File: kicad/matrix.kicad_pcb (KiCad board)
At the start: 2 copper layers, 7 parts, among them U1 TLC59025, U2 74HC595, U3 74HC595

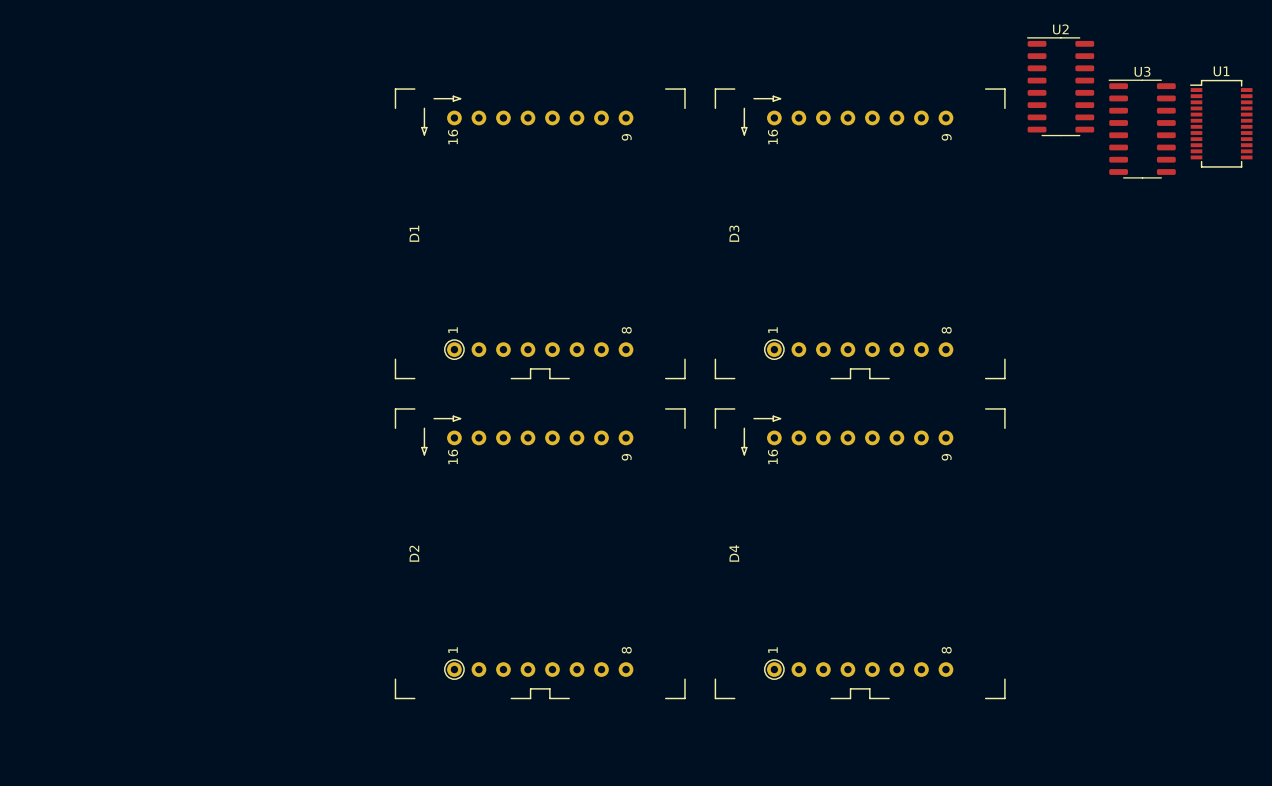
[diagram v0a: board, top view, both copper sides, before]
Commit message: Add footprints and initial layout
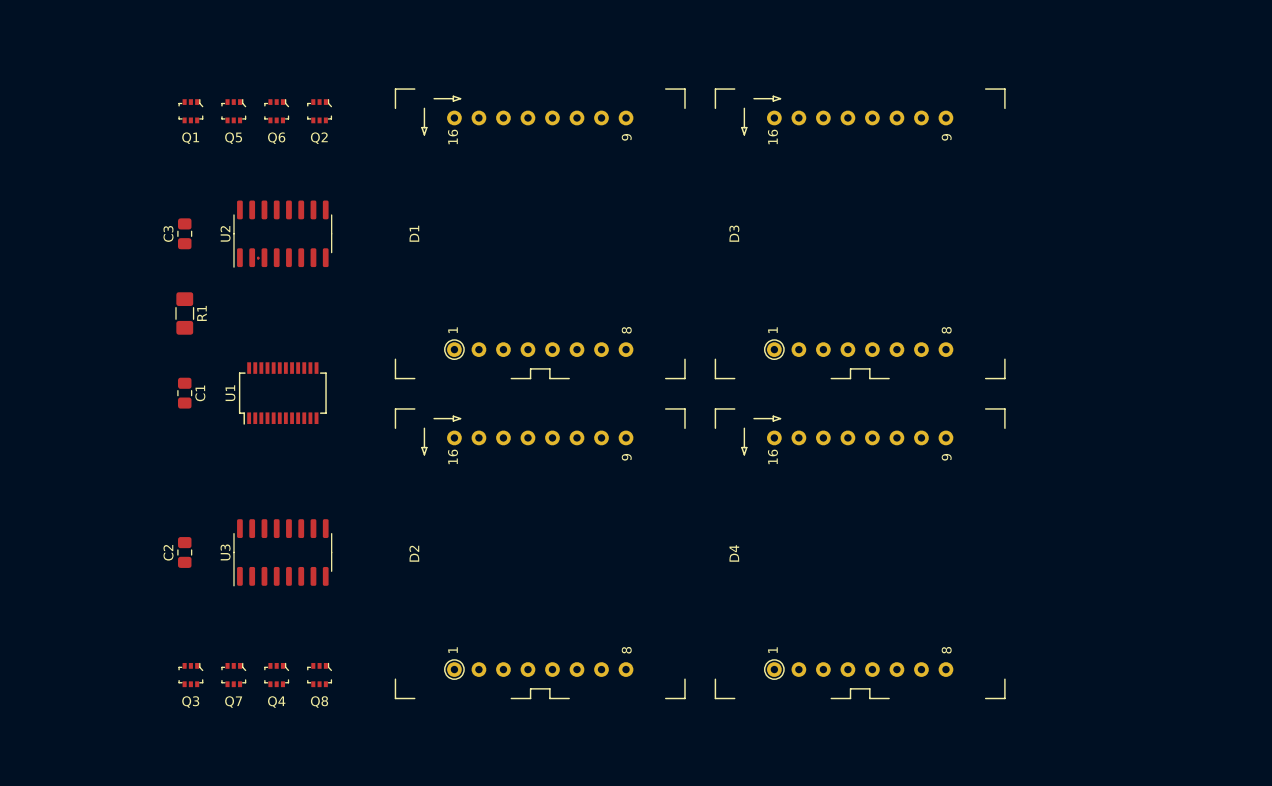
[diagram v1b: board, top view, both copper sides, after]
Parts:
- added C1: 100nF, Capacitor_SMD:C_0805_2012Metric_Pad1.15x1.40mm_HandSolder, F.Cu at (131.4, 75.6)
- added C2: 100nF, Capacitor_SMD:C_0805_2012Metric_Pad1.15x1.40mm_HandSolder, F.Cu at (131.4, 92.1)
- added C3: 100nF, Capacitor_SMD:C_0805_2012Metric_Pad1.15x1.40mm_HandSolder, F.Cu at (131.4, 59.1)
- added Q1: 2N7002DW-7-F, digikey-footprints:SOT-363, F.Cu at (132.1, 46.4)
- added Q2: 2N7002DW-7-F, digikey-footprints:SOT-363, F.Cu at (145.4, 46.4)
- added Q3: 2N7002DW-7-F, digikey-footprints:SOT-363, F.Cu at (132.1, 104.8)
- added Q4: 2N7002DW-7-F, digikey-footprints:SOT-363, F.Cu at (141.0, 104.8)
- added Q5: 2N7002DW-7-F, digikey-footprints:SOT-363, F.Cu at (136.5, 46.4)
- added Q6: 2N7002DW-7-F, digikey-footprints:SOT-363, F.Cu at (141.0, 46.4)
- added Q7: 2N7002DW-7-F, digikey-footprints:SOT-363, F.Cu at (136.5, 104.8)
- added Q8: 2N7002DW-7-F, digikey-footprints:SOT-363, F.Cu at (145.4, 104.8)
- added R1: 2.2K, Resistor_SMD:R_1206_3216Metric_Pad1.42x1.75mm_HandSolder, F.Cu at (131.4, 67.3)
- moved U1 101.2 mm to (141.6, 75.6), turned to 90 degrees
- moved U3 99.3 mm to (141.6, 92.1), turned to 90 degrees
- moved U2 82.0 mm to (141.6, 59.1), turned to 90 degrees
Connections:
- U2 pad 1: /ROW2 -> Net-(Q5-Pad2)
- U2 pad 15: /ROW1 -> Net-(Q1-Pad2)
- U2 pad 2: /ROW3 -> Net-(Q1-Pad5)
- U2 pad 3: /ROW4 -> Net-(Q5-Pad5)
- U2 pad 4: /ROW5 -> Net-(Q6-Pad2)
- U2 pad 5: /ROW6 -> Net-(Q2-Pad2)
- U2 pad 6: /ROW7 -> Net-(Q2-Pad5)
- U2 pad 7: /ROW8 -> Net-(Q6-Pad5)
- U3 pad 1: /ROW10 -> Net-(Q7-Pad2)
- U3 pad 15: /ROW9 -> Net-(Q3-Pad2)
- U3 pad 2: /ROW11 -> Net-(Q3-Pad5)
- U3 pad 3: /ROW12 -> Net-(Q7-Pad5)
- U3 pad 4: /ROW13 -> Net-(Q8-Pad2)
- U3 pad 5: /ROW14 -> Net-(Q4-Pad2)
- U3 pad 6: /ROW15 -> Net-(Q4-Pad5)
- U3 pad 7: /ROW16 -> Net-(Q8-Pad5)

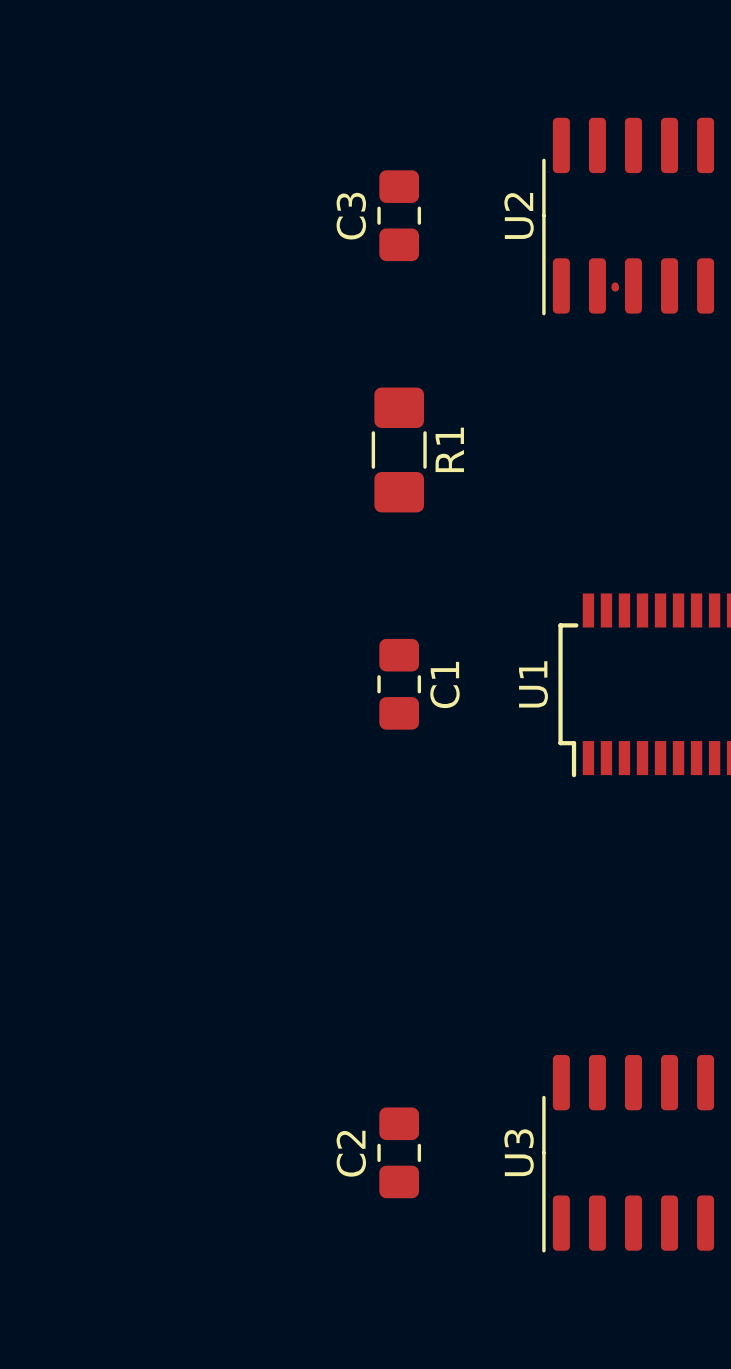
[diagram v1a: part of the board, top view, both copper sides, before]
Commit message: Add headers to PCB layout
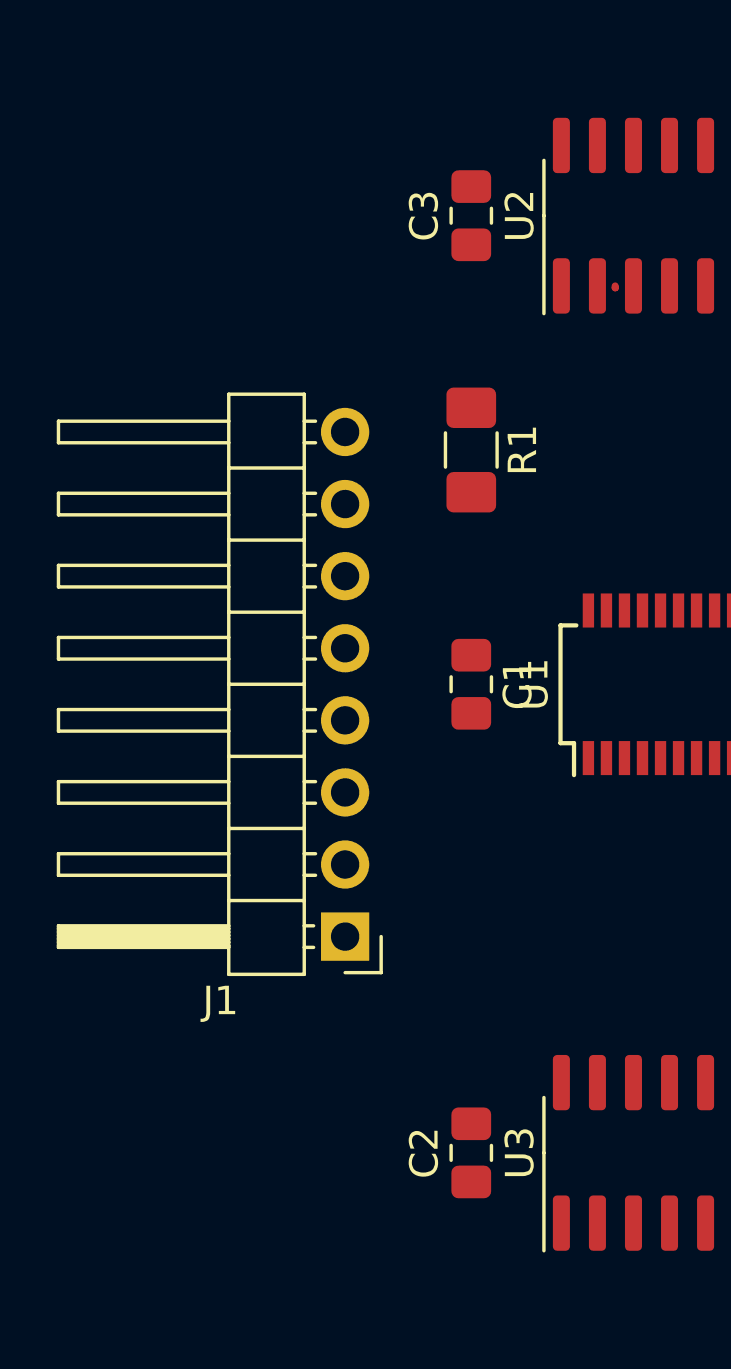
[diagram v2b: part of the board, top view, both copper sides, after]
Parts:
- added J1: Conn_01x08, Connector_PinHeader_2.54mm:PinHeader_1x08_P2.54mm_Horizontal, F.Cu at (129.5, 84.5)
- moved C1 2.54 mm to (134.0, 75.6)
- moved C2 2.54 mm to (134.0, 92.1)
- moved C3 2.54 mm to (134.0, 59.1)
- moved R1 2.54 mm to (134.0, 67.3)
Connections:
- net Net-(U2-Pad11) renamed /ROWCLK
- U1 pad 2: Net-(U1-Pad2) -> /COLSDI
- U1 pad 3: Net-(U1-Pad3) -> /COLCLK
- U1 pad 4: Net-(U1-Pad4) -> /LE
- U2 pad 10: Net-(U2-Pad10) -> VDD
- U2 pad 12: Net-(U2-Pad12) -> /LE
- U2 pad 14: Net-(U2-Pad14) -> /ROWSDI
- U3 pad 10: Net-(U2-Pad10) -> VDD
- U3 pad 12: Net-(U3-Pad12) -> /LE

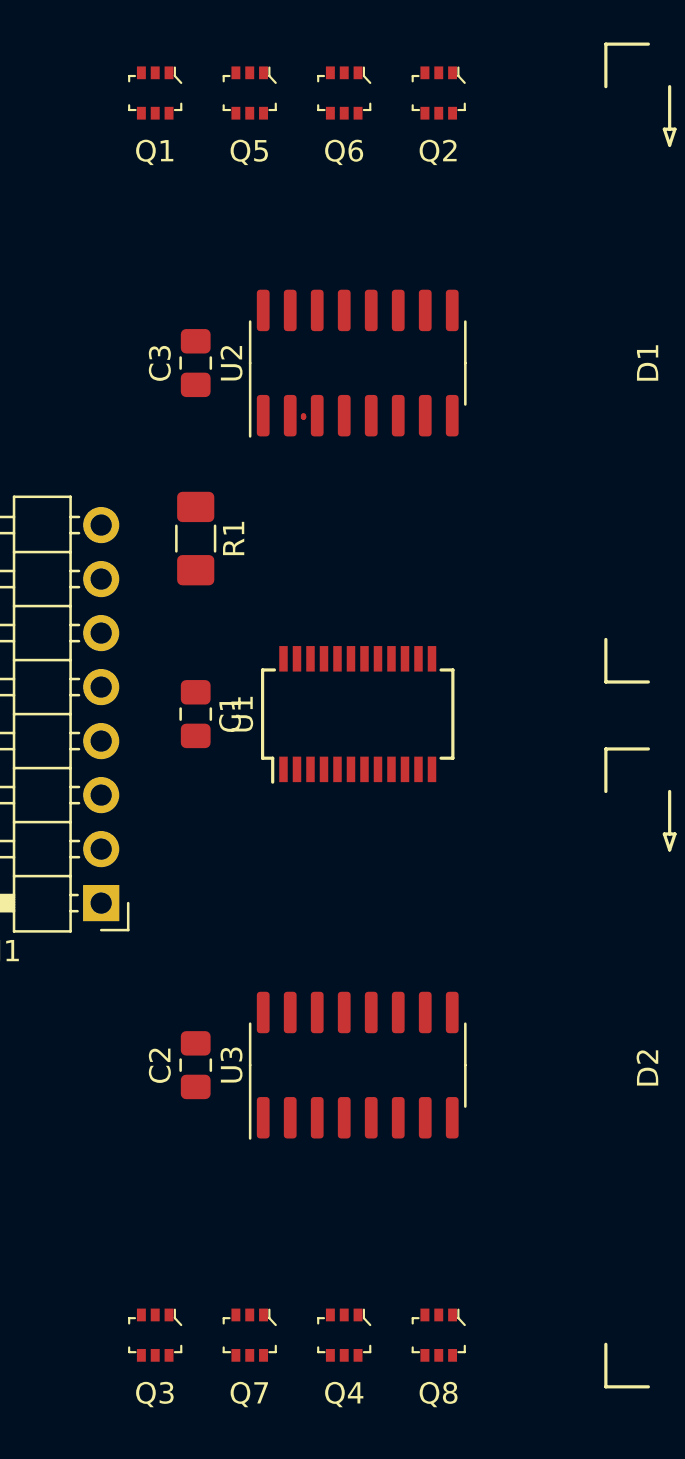
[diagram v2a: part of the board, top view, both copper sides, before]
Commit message: Add datasheets and long pad footprints
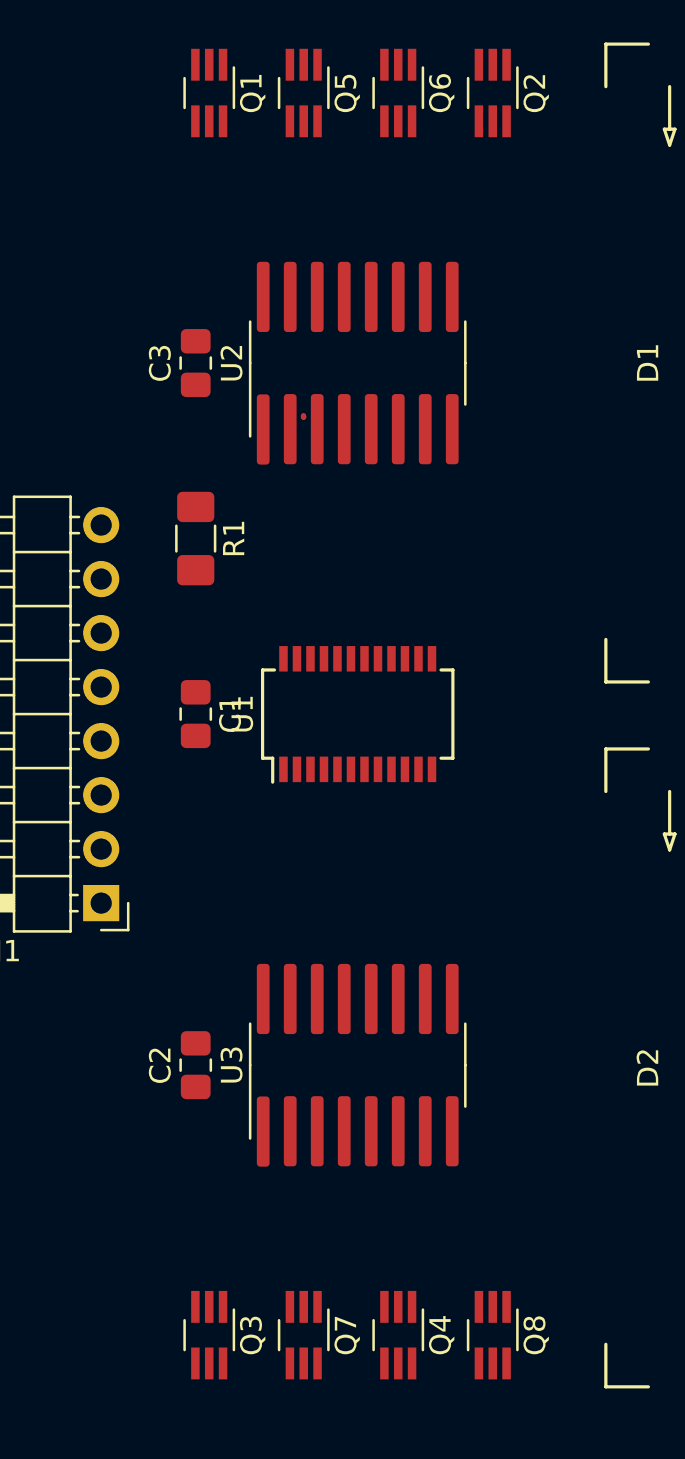
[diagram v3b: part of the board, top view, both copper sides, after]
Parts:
- Q1, Q2, Q3, Q4, Q5, Q6, Q7, Q8: footprint digikey-footprints:SOT-363 -> Package_TO_SOT_SMD:SOT-363_SC-70-6_Handsoldering
- U2, U3: footprint Package_SO:SOIC-16_3.9x9.9mm_P1.27mm -> local:SOIC-16_3.9x9.9mm_P1.27mm_widepads
- moved Q2 2.54 mm to (148.0, 46.4), turned to 270 degrees
- moved Q8 2.54 mm to (148.0, 104.8), turned to 270 degrees
- moved Q1 2.54 mm to (134.6, 46.4), turned to 270 degrees
- moved Q3 2.54 mm to (134.6, 104.8), turned to 270 degrees
- moved Q4 2.54 mm to (143.5, 104.8), turned to 270 degrees
- moved Q5 2.54 mm to (139.1, 46.4), turned to 270 degrees
- moved Q6 2.54 mm to (143.5, 46.4), turned to 270 degrees
- moved Q7 2.54 mm to (139.1, 104.8), turned to 270 degrees

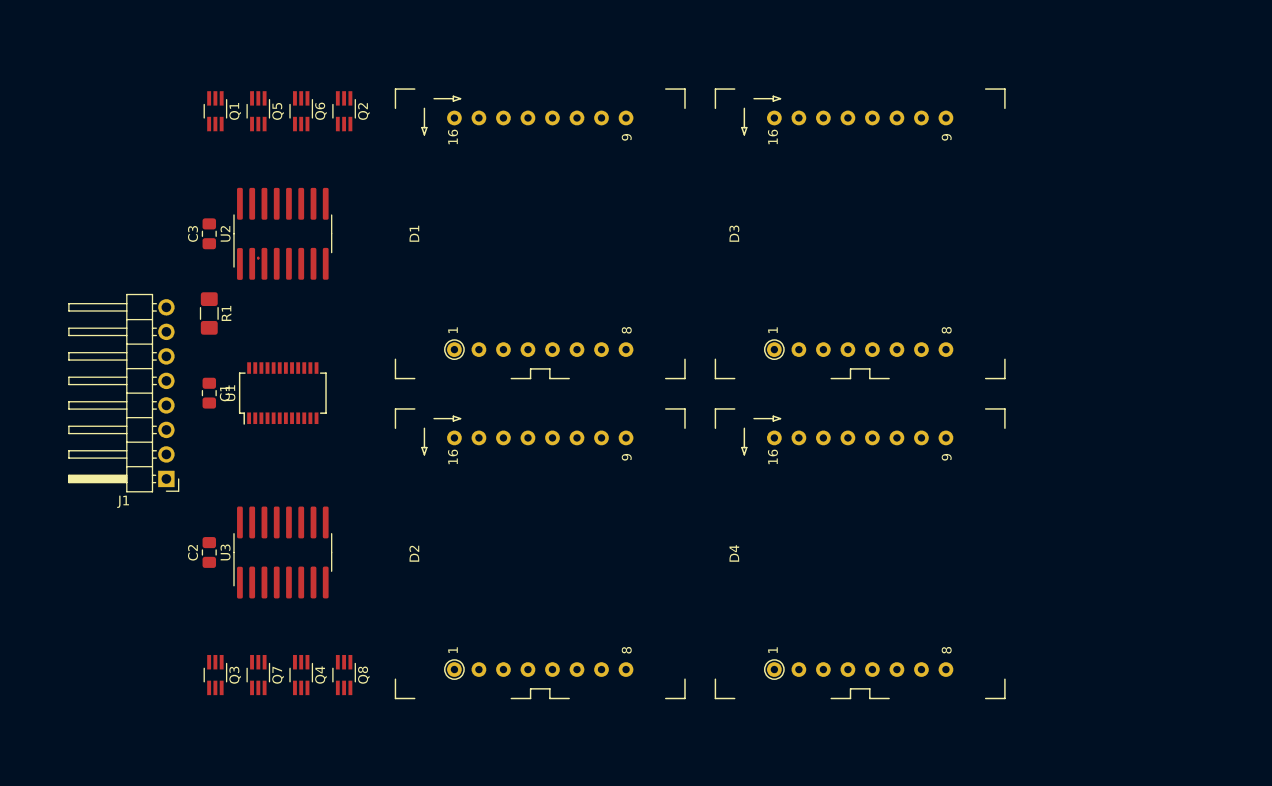
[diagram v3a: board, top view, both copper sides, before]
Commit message: Enlarge display footprint and SMD pad widths
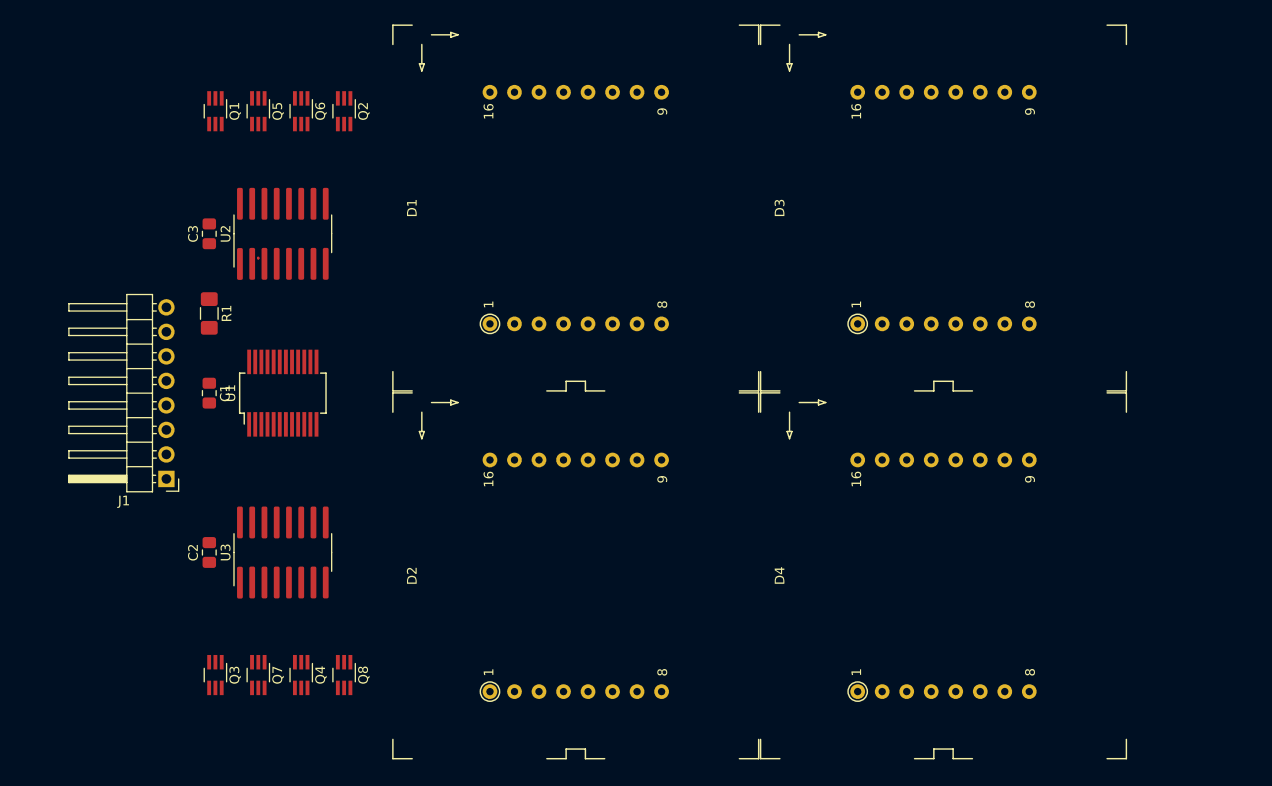
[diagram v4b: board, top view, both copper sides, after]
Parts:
- D1, D2, D3, D4: footprint akn_misc:LED_8x8_3MM_32x32MM -> local:LED_8x8_3MM_38x38MM
- U1: footprint Package_SO:SSOP-24_3.9x8.7mm_P0.635mm -> local:SSOP-24_3.9x8.7mm_P0.635mm_widepads
- moved D3 9.04 mm to (210.1, 56.4)
- moved D4 8.93 mm to (210.1, 94.5)
- moved D1 4.55 mm to (172.0, 56.4)
- moved D2 4.33 mm to (172.0, 94.5)
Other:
- rule pad_to_mask_clearance: 0.051 -> 0.0508
- rule solder_mask_min_width: 0.25 -> 0.1016
